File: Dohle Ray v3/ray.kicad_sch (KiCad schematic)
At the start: 32 parts, among them J1 Conn_01x07_Female, J2 AudioJack3, J3 AudioJack3, Q1 J201, SW1 3pdt_footswitch, U1 TL082

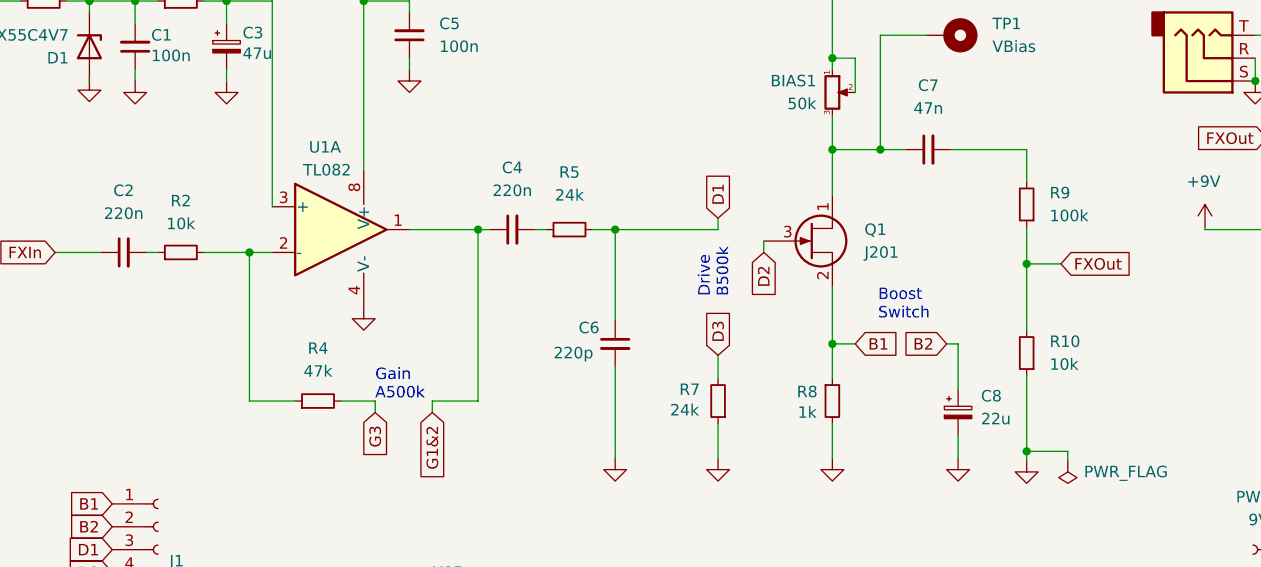
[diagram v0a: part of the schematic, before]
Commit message: Update resistor values
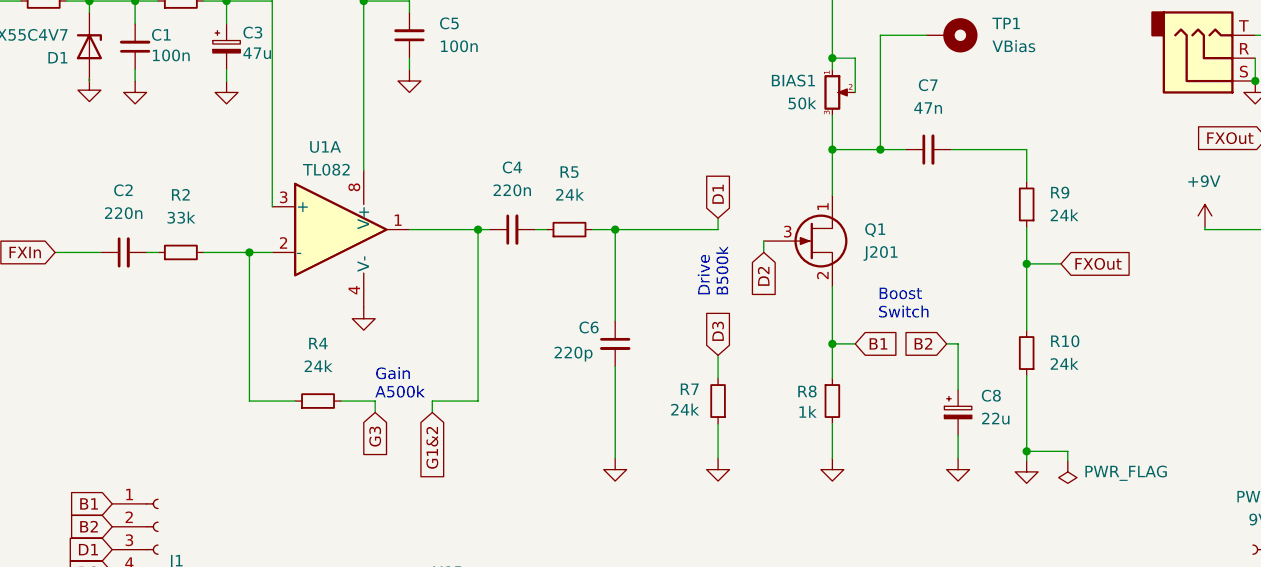
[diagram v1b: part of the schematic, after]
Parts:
- R10: value 10k -> 24k
- R2: value 10k -> 33k
- R4: value 47k -> 24k
- R9: value 100k -> 24k
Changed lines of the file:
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@@
       (effects (font (size 1.27 1.27)) (justify right))
     )
-    (property "Value" "10k" (id 1) (at 133.35 68.3259 0)
+    (property "Value" "24k" (id 1) (at 133.35 68.3259 0)
       (effects (font (size 1.27 1.27)) (justify right))
     )
@@
       (effects (font (size 1.27 1.27)) (justify right))
     )
-    (property "Value" "100k" (id 1) (at 133.35 51.8159 0)
+    (property "Value" "24k" (id 1) (at 133.35 51.8159 0)
       (effects (font (size 1.27 1.27)) (justify right))
     )
@@
   (symbol (lib_id "Device:R_Small") (at 36.83 55.88 90) (unit 1)
     (in_bom yes) (on_board yes) (fields_autoplaced)
-    (property "Reference" "R2" (id 0) (at 36.83 50.165 90))
-    (property "Value" "10k" (id 1) (at 36.83 52.705 90))
+    (property "Reference" "R2" (id 0) (at 36.83 49.53 90))
+    (property "Value" "33k" (id 1) (at 36.83 52.07 90))
     (property "Footprint" "Resistor_THT:R_Axial_DIN0207_L6.3mm_D2.5mm_P10.16mm_Horizontal" (id 2) (at 36.83 55.88 0)
       (effects (font (size 1.27 1.27)) hide)
@@
   (symbol (lib_id "Device:R_Small") (at 52.07 72.39 90) (unit 1)
     (in_bom yes) (on_board yes) (fields_autoplaced)
-    (property "Reference" "R4" (id 0) (at 52.07 66.548 90))
-    (property "Value" "47k" (id 1) (at 52.07 69.088 90))
+    (property "Reference" "R4" (id 0) (at 52.07 66.04 90))
+    (property "Value" "24k" (id 1) (at 52.07 68.58 90))
     (property "Footprint" "Resistor_THT:R_Axial_DIN0207_L6.3mm_D2.5mm_P10.16mm_Horizontal" (id 2) (at 52.07 72.39 0)
       (effects (font (size 1.27 1.27)) hide)
@@
     )
     (path "/a92599f6-8e7a-4af0-94bd-cf879288cb6a"
-      (reference "R2") (unit 1) (value "10k") (footprint "Resistor_THT:R_Axial_DIN0207_L6.3mm_D2.5mm_P10.16mm_Horizontal")
+      (reference "R2") (unit 1) (value "33k") (footprint "Resistor_THT:R_Axial_DIN0207_L6.3mm_D2.5mm_P10.16mm_Horizontal")
     )
     (path "/21fbe1aa-b8a9-42fe-a829-c03aab0f6e55"
@@
     )
     (path "/db65d6cf-b8af-4ae7-be89-6cb02b218eac"
-      (reference "R4") (unit 1) (value "47k") (footprint "Resistor_THT:R_Axial_DIN0207_L6.3mm_D2.5mm_P10.16mm_Horizontal")
+      (reference "R4") (unit 1) (value "24k") (footprint "Resistor_THT:R_Axial_DIN0207_L6.3mm_D2.5mm_P10.16mm_Horizontal")
     )
     (path "/e9306d17-673c-4f61-9462-fdbbdb029457"
@@
     )
     (path "/7cafa446-00e0-4641-9b9f-19c6ccc5577a"
-      (reference "R9") (unit 1) (value "100k") (footprint "Resistor_THT:R_Axial_DIN0207_L6.3mm_D2.5mm_P10.16mm_Horizontal")
+      (reference "R9") (unit 1) (value "24k") (footprint "Resistor_THT:R_Axial_DIN0207_L6.3mm_D2.5mm_P10.16mm_Horizontal")
     )
     (path "/035ae7b8-9555-4334-a7f9-f84468496b25"
-      (reference "R10") (unit 1) (value "10k") (footprint "Resistor_THT:R_Axial_DIN0207_L6.3mm_D2.5mm_P10.16mm_Horizontal")
+      (reference "R10") (unit 1) (value "24k") (footprint "Resistor_THT:R_Axial_DIN0207_L6.3mm_D2.5mm_P10.16mm_Horizontal")
     )
     (path "/1f6adf16-21d7-423b-b144-d3a750b26611"

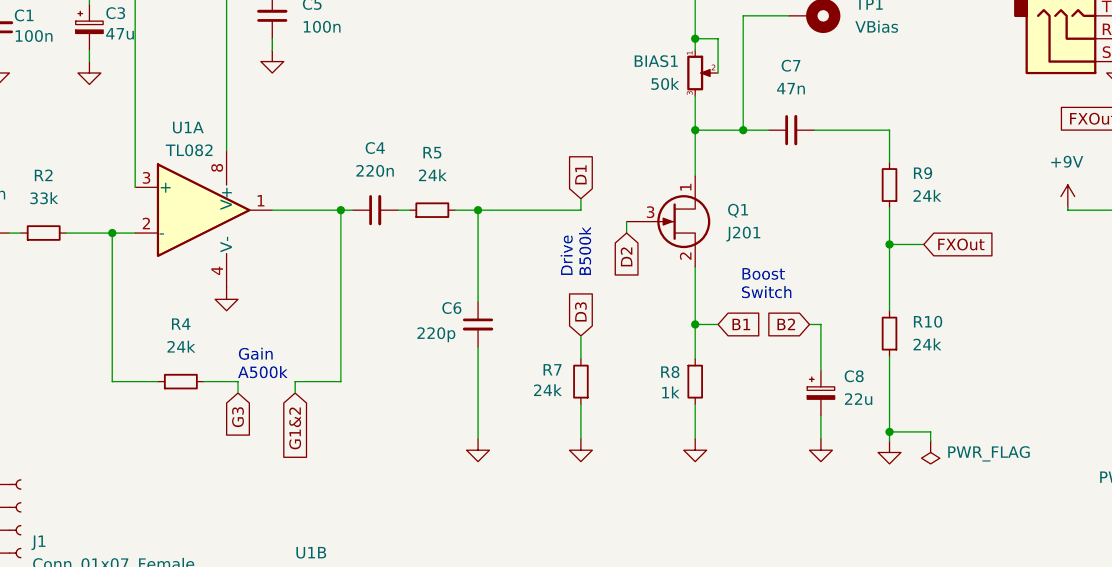
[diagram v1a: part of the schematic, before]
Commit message: Update resistor values to have unity gain at 0% volume and gain knob, update PCB revision
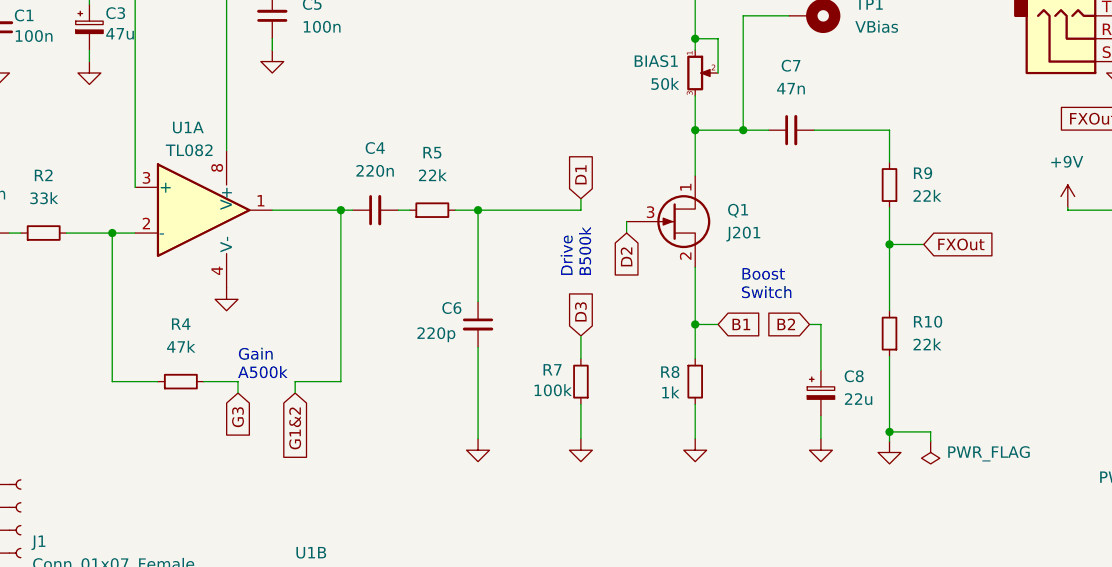
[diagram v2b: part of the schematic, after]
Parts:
- R10, R5, R9: value 24k -> 22k
- R4: value 24k -> 47k
- R7: value 24k -> 100k
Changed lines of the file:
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@@
       (effects (font (size 1.27 1.27)) (justify right))
     )
-    (property "Value" "24k" (id 1) (at 133.35 68.3259 0)
+    (property "Value" "22k" (id 1) (at 133.35 68.3259 0)
       (effects (font (size 1.27 1.27)) (justify right))
     )
@@
       (effects (font (size 1.27 1.27)) (justify right))
     )
-    (property "Value" "24k" (id 1) (at 91.186 73.406 0)
+    (property "Value" "100k" (id 1) (at 91.186 73.406 0)
       (effects (font (size 1.27 1.27)) (justify right))
     )
@@
       (effects (font (size 1.27 1.27)) (justify right))
     )
-    (property "Value" "24k" (id 1) (at 133.35 51.8159 0)
+    (property "Value" "22k" (id 1) (at 133.35 51.8159 0)
       (effects (font (size 1.27 1.27)) (justify right))
     )
@@
     (in_bom yes) (on_board yes) (fields_autoplaced)
     (property "Reference" "R4" (id 0) (at 52.07 66.04 90))
-    (property "Value" "24k" (id 1) (at 52.07 68.58 90))
+    (property "Value" "47k" (id 1) (at 52.07 68.58 90))
     (property "Footprint" "Resistor_THT:R_Axial_DIN0207_L6.3mm_D2.5mm_P10.16mm_Horizontal" (id 2) (at 52.07 72.39 0)
       (effects (font (size 1.27 1.27)) hide)
@@
     (in_bom yes) (on_board yes) (fields_autoplaced)
     (property "Reference" "R5" (id 0) (at 80.01 46.99 90))
-    (property "Value" "24k" (id 1) (at 80.01 49.53 90))
+    (property "Value" "22k" (id 1) (at 80.01 49.53 90))
     (property "Footprint" "Resistor_THT:R_Axial_DIN0207_L6.3mm_D2.5mm_P10.16mm_Horizontal" (id 2) (at 80.01 53.34 0)
       (effects (font (size 1.27 1.27)) hide)
@@
     )
     (path "/db65d6cf-b8af-4ae7-be89-6cb02b218eac"
-      (reference "R4") (unit 1) (value "24k") (footprint "Resistor_THT:R_Axial_DIN0207_L6.3mm_D2.5mm_P10.16mm_Horizontal")
+      (reference "R4") (unit 1) (value "47k") (footprint "Resistor_THT:R_Axial_DIN0207_L6.3mm_D2.5mm_P10.16mm_Horizontal")
     )
     (path "/e9306d17-673c-4f61-9462-fdbbdb029457"
-      (reference "R5") (unit 1) (value "24k") (footprint "Resistor_THT:R_Axial_DIN0207_L6.3mm_D2.5mm_P10.16mm_Horizontal")
+      (reference "R5") (unit 1) (value "22k") (footprint "Resistor_THT:R_Axial_DIN0207_L6.3mm_D2.5mm_P10.16mm_Horizontal")
     )
     (path "/0bdd6155-568e-469f-8641-16545d79c806"
@@
     )
     (path "/27ea7bc3-87d8-41e5-8b85-39ee481a49f1"
-      (reference "R7") (unit 1) (value "24k") (footprint "Resistor_THT:R_Axial_DIN0207_L6.3mm_D2.5mm_P10.16mm_Horizontal")
+      (reference "R7") (unit 1) (value "100k") (footprint "Resistor_THT:R_Axial_DIN0207_L6.3mm_D2.5mm_P10.16mm_Horizontal")
     )
     (path "/d7e14f87-889d-4cc4-a810-86aef18e0af8"
@@
     )
     (path "/7cafa446-00e0-4641-9b9f-19c6ccc5577a"
-      (reference "R9") (unit 1) (value "24k") (footprint "Resistor_THT:R_Axial_DIN0207_L6.3mm_D2.5mm_P10.16mm_Horizontal")
+      (reference "R9") (unit 1) (value "22k") (footprint "Resistor_THT:R_Axial_DIN0207_L6.3mm_D2.5mm_P10.16mm_Horizontal")
     )
     (path "/035ae7b8-9555-4334-a7f9-f84468496b25"
-      (reference "R10") (unit 1) (value "24k") (footprint "Resistor_THT:R_Axial_DIN0207_L6.3mm_D2.5mm_P10.16mm_Horizontal")
+      (reference "R10") (unit 1) (value "22k") (footprint "Resistor_THT:R_Axial_DIN0207_L6.3mm_D2.5mm_P10.16mm_Horizontal")
     )
     (path "/1f6adf16-21d7-423b-b144-d3a750b26611"
